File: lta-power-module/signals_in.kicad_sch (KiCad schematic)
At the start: 87 parts

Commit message: Small sheet cleanup.
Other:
- note added: "${REV_DATE}"
- note added: "${REV}"
- note added: "Signal input processing from logic module"
- note added: "Signal inverter and 3V3-to-12V0 voltage shifter"
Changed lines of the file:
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@@
+    (effects (font (size 1.27 1.27)) (justify left bottom))
+  )
+  (text "${REV}\n" (at 268.605 194.31 0)
     (effects (font (size 1.27 1.27)) (justify left bottom))
   )
@@
     (at 18.415 150.495 0)
     (effects (font (size 1.27 1.27)) (justify left bottom))
+  )
+  (text "Signal inverter and 3V3-to-12V0 voltage shifter" (at 180.34 175.895 0)
+    (effects (font (size 2.54 2.54)) (justify left bottom))
   )
   (text "12V from bank 0 regulator" (at 33.02 20.955 0)
@@
     (effects (font (size 1.27 1.27)) (justify left bottom))
   )
+  (text "Signal input processing from logic module" (at 186.69 190.5 0)
+    (effects (font (size 1.27 1.27)) (justify left bottom))
+  )
+  (text "${REV_DATE}" (at 207.01 194.31 0)
+    (effects (font (size 1.27 1.27)) (justify left bottom))
+  )

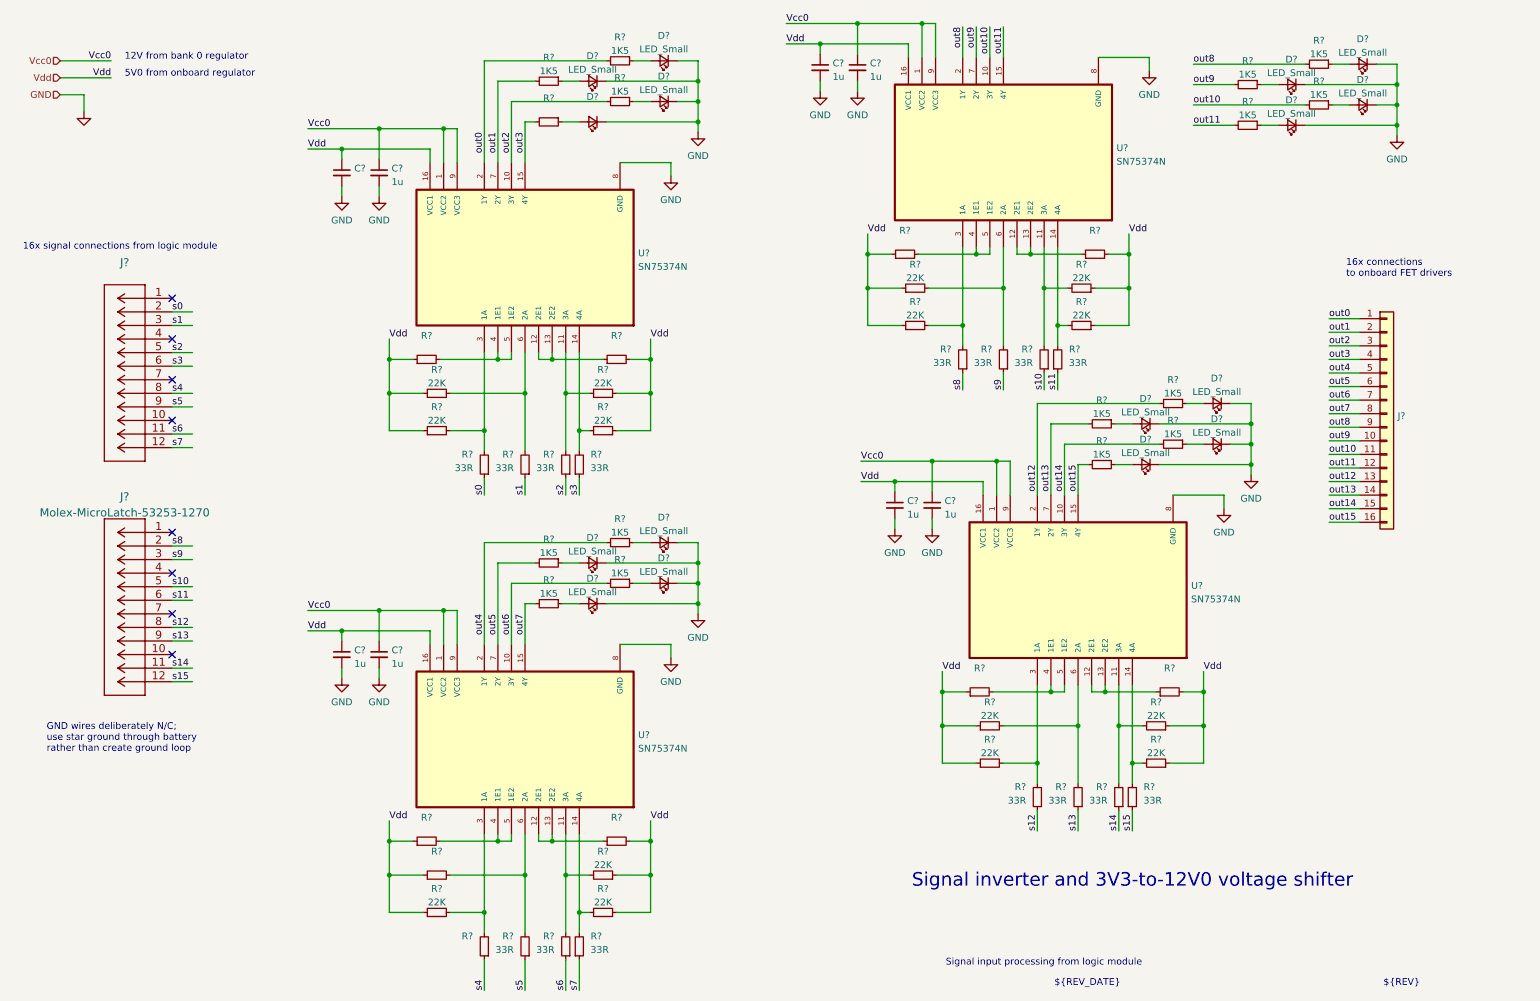
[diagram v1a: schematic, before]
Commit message: Add custom footprints for 12V regulator and power distribution bus.
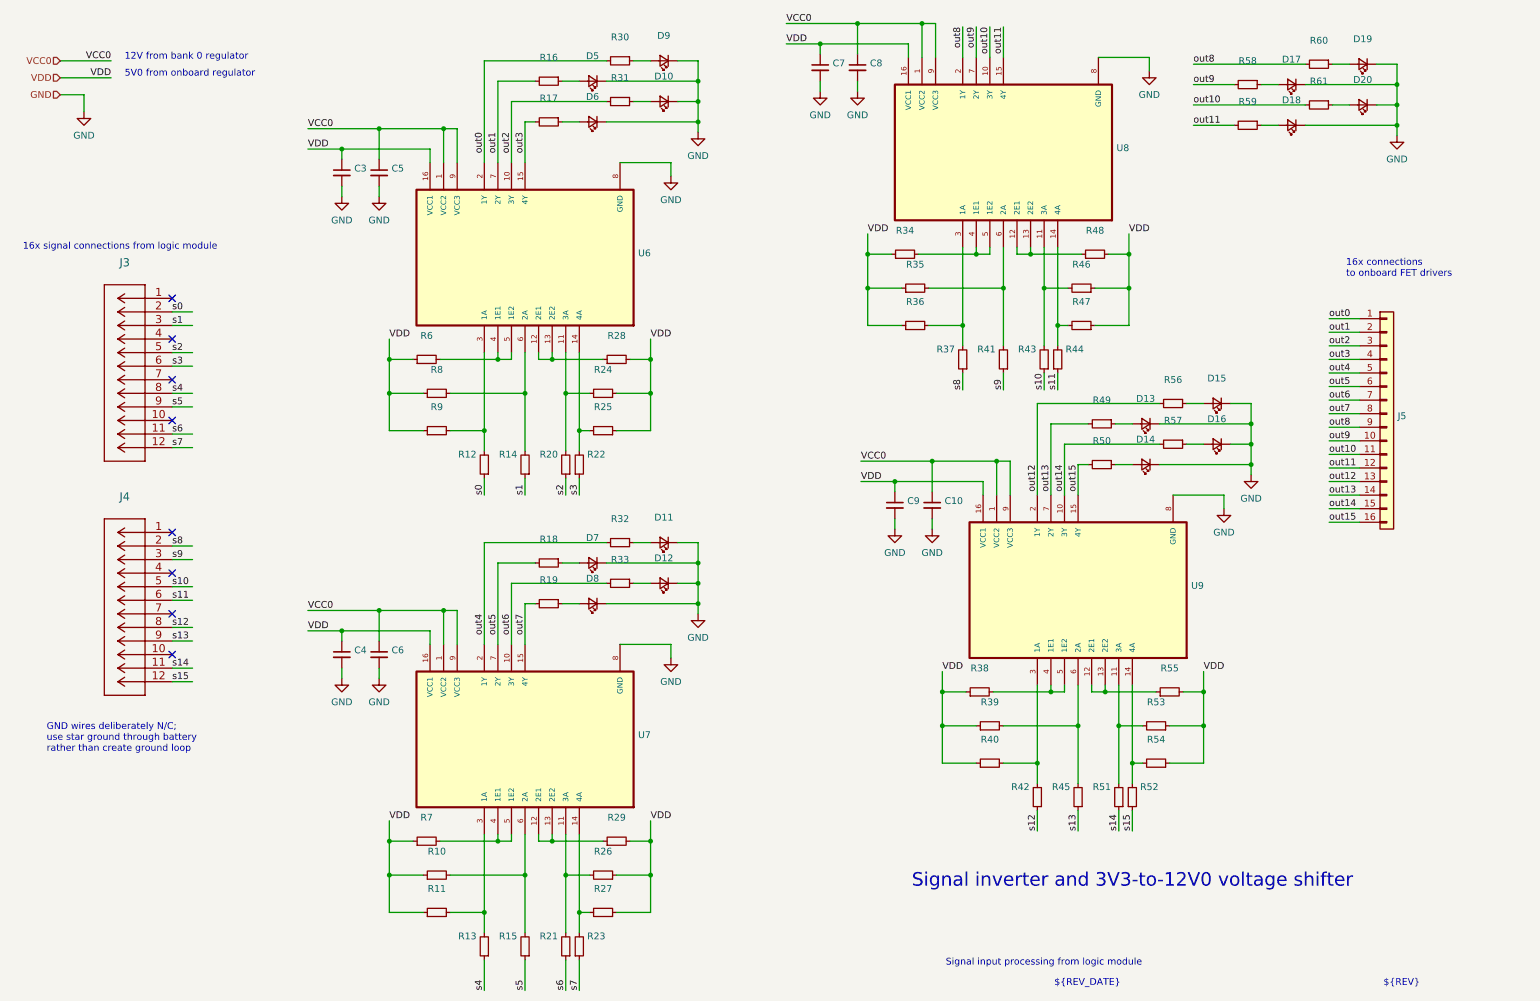
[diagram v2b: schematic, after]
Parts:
- C10, C4, C5, C6, C7, C8, C9: renamed from C?; value 1u -> (none); Comment (none) -> 1u X7R 25V low-ESR THT; MANUFACTURER (none) -> KEMET; MPN (none) -> C315C105K3R5TA7303
- C3: renamed from C?; Comment (none) -> 1u X7R 25V low-ESR THT; MANUFACTURER (none) -> KEMET; MPN (none) -> C315C105K3R5TA7303
- D10, D11, D12, D13, D14, D15, D16, D17, D18, D19, D20, D5, D7, D8, D9: renamed from D?; value LED_Small -> (none); Comment (none) -> Vf=1.7V I_test=20mA yellow LED 5mm THT; MANUFACTURER (none) -> Everlight; MPN (none) -> EALP05RDHYA0
- D6: renamed from D?; Comment (none) -> Vf=1.7V I_test=20mA yellow LED 5mm THT; MANUFACTURER (none) -> Everlight; MPN (none) -> EALP05RDHYA0
- J4: renamed from J?; value Molex-MicroLatch-53253-1270 -> (none); footprint Aaron_THT:Molex-MicroLatch-53253-1270 -> (none)
- R10: renamed from R?; Comment (none) -> 22K THT resistor; +/-5%; 1/8W; MANUFACTURER (none) -> Stackpole; MPN (none) -> CF18JT22K0
- R11, R24, R25, R26, R27, R35, R36, R39, R40, R46, R47, R53, R54, R8, R9: renamed from R?; value 22K -> (none); Comment (none) -> 22K THT resistor; +/-5%; 1/8W; MANUFACTURER (none) -> Stackpole; MPN (none) -> CF18JT22K0
- R12, R14, R15, R20, R21, R22, R23, R37, R41, R42, R43, R44, R45, R51, R52: renamed from R?; value 33R -> (none); Comment (none) -> 33R THT resistor; +/-5%; 1/8W; MANUFACTURER (none) -> Stackpole; MPN (none) -> CF18JT33R0
- R13: renamed from R?; Comment (none) -> 33R THT resistor; +/-5%; 1/8W; MANUFACTURER (none) -> Stackpole; MPN (none) -> CF18JT33R0
- R16, R18, R19, R30, R31, R32, R33, R49, R50, R56, R57, R58, R59, R60, R61: renamed from R?; value 1K5 -> (none); Comment (none) -> 1K5 THT resistor; +/-5%; 1/8W; MANUFACTURER (none) -> Stackpole; MPN (none) -> CF18JT1K50
- R17: renamed from R?; Comment (none) -> 1K5 THT resistor; +/-5%; 1/8W; MANUFACTURER (none) -> Stackpole; MPN (none) -> CF18JT1K50
- R28, R29, R34, R38, R48, R55, R6, R7: renamed from R?; Comment (none) -> 470R THT resistor; +/-5%; 1/8W; MANUFACTURER (none) -> Stackpole; MPN (none) -> CF18JT470R0
- U6, U7, U8, U9: renamed from U?; value SN75374N -> (none); footprint Aaron_TI_Parts:TI_N_R-PDIP-T16 -> (none); MANUFACTURER (none) -> Texas Instruments; MPN (none) -> SN75374N
- gave numbers to parts that had none: 2
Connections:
- net Vcc0 renamed VCC0
- net Vdd renamed VDD

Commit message: Remove unnecessary LEDs.
The MOSFET drivers have LEDs which will operate based on the gate
signal alone; we can just rely on those.
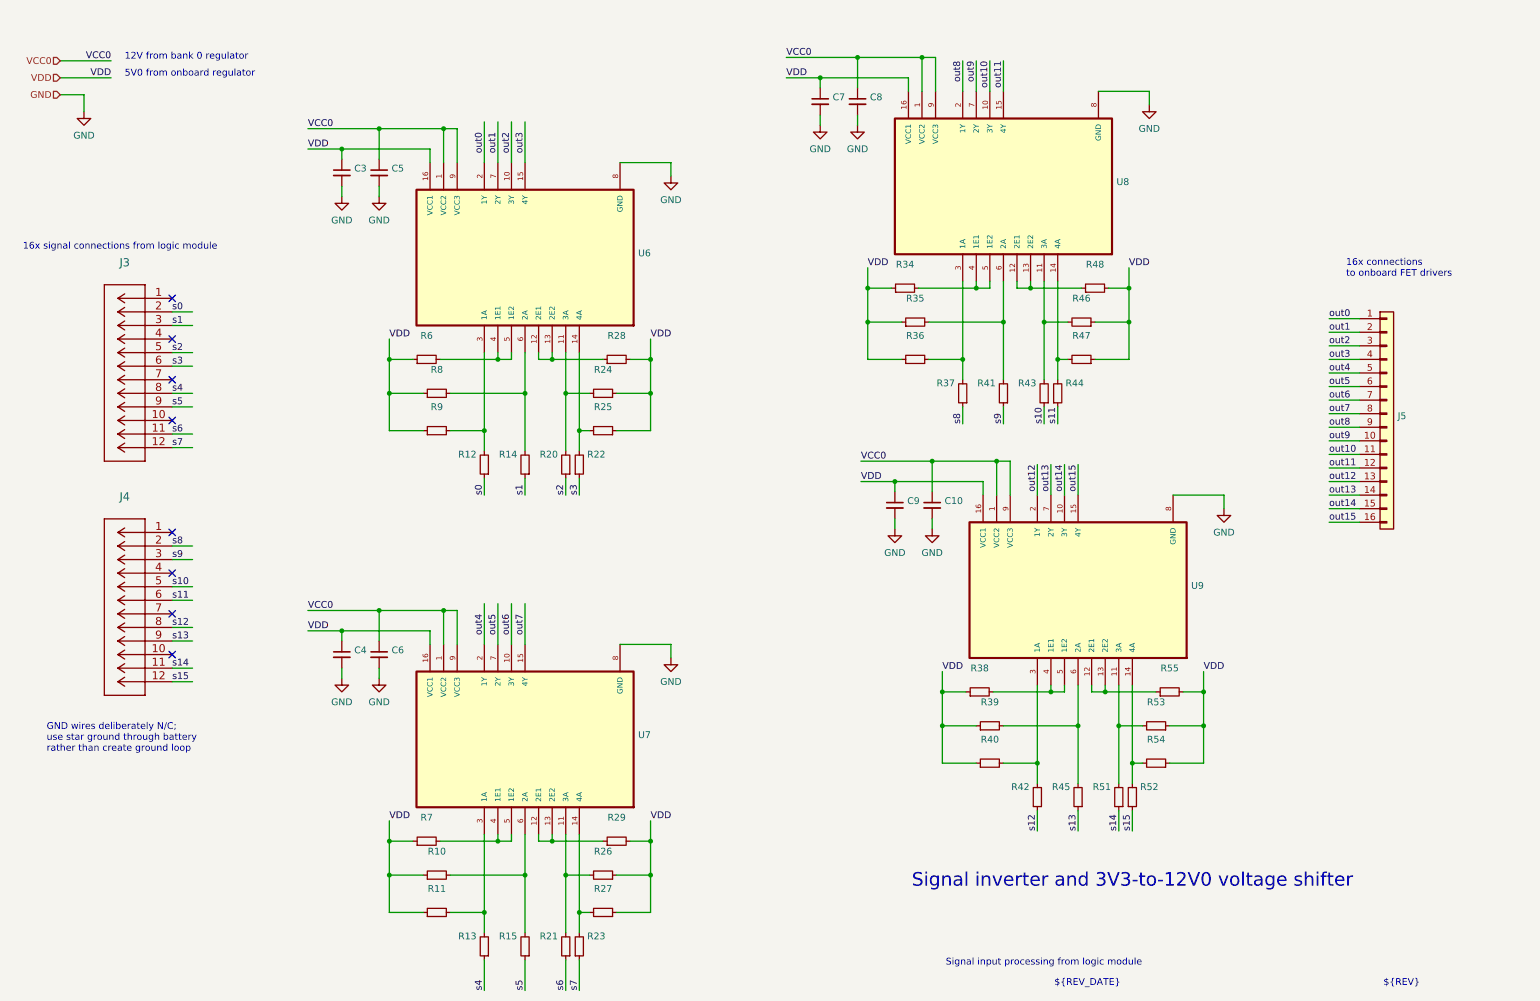
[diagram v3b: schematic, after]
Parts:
- removed D10, D11, D12, D13, D14, D15, D16, D17, D18, D19, D20, D5, D6, D7, D8, D9: (no value), symbol Device:LED_Small
- removed R16, R17, R18, R19, R30, R31, R32, R33, R49, R50, R56, R57, R58, R59, R60, R61: (no value), symbol Device:R_Small
- J5: Comment (none) -> standard male 2.54mm gold THT header pin row
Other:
- moved on the sheet: C7, C8, R34, R35, R36, R37, R41, R43, R44, R46, R47, R48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
